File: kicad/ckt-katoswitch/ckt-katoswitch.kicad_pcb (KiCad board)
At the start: 2 copper layers, 76.2 x 63.5 mm, 50 parts, among them J1 SM04B-SRSS, J10 SM04B-SRSS, J11 Conn_AVR_TagConnect_TC2030, J2 SM04B-SRSS, J3 SM04B-SRSS, J4 SM04B-SRSS, J5 SM04B-SRSS, J6 SM04B-SRSS, J7 SM04B-SRSS, J8 SM04B-SRSS, J9 SM04B-SRSS, Q1 ZXMS6004FF, SW1 SW_DIP_x05, U1 AP7381-33Y, U2 ATtiny861A-S

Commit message: Initial cut at PCB
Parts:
- removed C10, C5, C8: 1uF, Capacitor_SMD:C_0805_2012Metric
- removed C9: 0.1uF, Capacitor_SMD:C_0805_2012Metric
- removed J10, J8, J9: SM04B-SRSS, Connector_JST:JST_SH_SM04B-SRSS-TB_1x04-1MP_P1.00mm_Horizontal
- removed J11: Conn_AVR_TagConnect_TC2030, Connector:Tag-Connect_TC2030-IDC-NL_2x03_P1.27mm_Vertical
- removed R10, R11, R6, R7, R8: 1k, Resistor_SMD:R_0805_2012Metric
- removed R9: 10k, Resistor_SMD:R_0805_2012Metric
- removed SW1: SW_DIP_x05, ISE_UltraLibrarian:CST_219SMT
- removed TP1, TP2, TP3, TP4, TP5, TP6: TestPoint, TestPoint:TestPoint_Pad_D2.0mm
- added D5: AMBER, LED_SMD:LED_0805_2012Metric, F.Cu at (34.5, 46.4)
- added D6: GREEN LED, LED_SMD:LED_0805_2012Metric, F.Cu at (70.7, 35.3)
- added D7: BLUE, LED_SMD:LED_0805_2012Metric, F.Cu at (30.6, 46.4)
- added D8: AMBER, LED_SMD:LED_0805_2012Metric, F.Cu at (65.9, 58.3)
- added JP1: SolderJumper_2_Open, Jumper:SolderJumper-2_P1.3mm_Open_RoundedPad1.0x1.5mm, F.Cu at (64.1, 63.7)
- added JP2: SolderJumper_2_Open, Jumper:SolderJumper-2_P1.3mm_Open_RoundedPad1.0x1.5mm, F.Cu at (64.1, 68.3)
- added JP3: SolderJumper_2_Open, Jumper:SolderJumper-2_P1.3mm_Open_RoundedPad1.0x1.5mm, F.Cu at (64.1, 72.9)
- added K1: AGQ200A4H, ISE_UltraLibrarian:RELAY_AGQ_A_PAN, F.Cu at (32.6, 55.5)
- added U3: ATtiny414-SS, Package_SO:SOIC-14_3.9x8.7mm_P1.27mm, F.Cu at (49.9, 54.1)
- added U4: LTV-357T, Package_SO:SO-4_4.4x3.6mm_P2.54mm, F.Cu at (59.6, 58.2)
- C1: value 10uF -> 68uF; footprint Capacitor_SMD:C_0805_2012Metric -> Capacitor_SMD:CP_Elec_6.3x5.8
- C2: value 22uF -> 10uF
- C4: value 1uF -> 22uF
- D1: value GREEN LED -> CDBM140G; footprint LED_SMD:LED_0805_2012Metric -> ISE_Generic:SOD-123T
- D2: value RED -> CDBM140G; footprint LED_SMD:LED_0805_2012Metric -> ISE_Generic:SOD-123T
- D3, D4: value AMBER -> CDBM140G; footprint LED_SMD:LED_0805_2012Metric -> ISE_Generic:SOD-123T
- J1, J2: value SM04B-SRSS -> Screw_Terminal_01x02; footprint Connector_JST:JST_SH_SM04B-SRSS-TB_1x04-1MP_P1.00mm_Horizontal -> TerminalBlock_RND:TerminalBlock_RND_205-00012_1x02_P5.00mm_Horizontal
- J3: value SM04B-SRSS -> Conn_AVR_TagConnect_TC2030; footprint Connector_JST:JST_SH_SM04B-SRSS-TB_1x04-1MP_P1.00mm_Horizontal -> Connector:Tag-Connect_TC2030-IDC-NL_2x03_P1.27mm_Vertical
- J4, J5, J6: value SM04B-SRSS -> Screw_Terminal_01x02; footprint Connector_JST:JST_SH_SM04B-SRSS-TB_1x04-1MP_P1.00mm_Horizontal -> TerminalBlock_MetzConnect:TerminalBlock_MetzConnect_Type059_RT06303HBWC_1x03_P3.50mm_Horizontal
- J7: value SM04B-SRSS -> Conn_01x03; footprint Connector_JST:JST_SH_SM04B-SRSS-TB_1x04-1MP_P1.00mm_Horizontal -> Connector_PinHeader_2.54mm:PinHeader_1x03_P2.54mm_Vertical
- Q1: value ZXMS6004FF -> DRDC3105-7
- U1: value AP7381-33Y -> AP7381-50Y
- U2: value ATtiny861A-S -> DRV8231A; footprint Package_SO:SOIC-20W_7.5x12.8mm_P1.27mm -> Package_SO:Texas_HTSOP-8-1EP_3.9x4.9mm_P1.27mm_EP2.95x4.9mm_Mask2.4x3.1mm_ThermalVias
- moved H2 67.9 mm to (29.7, 71.9)
- moved H4 64.3 mm to (71.9, 29.7)
- moved J5 55.8 mm to (36.9, 69.0), turned to 0 degrees
- moved H3 54.8 mm to (71.9, 71.9)
- moved J4 46.4 mm to (49.7, 69.0), turned to 0 degrees
- moved J7 44.2 mm to (66.3, 40.9), turned to 90 degrees
- moved D4 41.3 mm to (51.6, 34.5), turned to 180 degrees
- moved J1 37.0 mm to (64.9, 32.6), turned to 180 degrees
- moved R2 35.4 mm to (40.0, 44.7), turned to 0 degrees
- moved D3 35.0 mm to (51.6, 38.0), turned to 180 degrees
- moved J6 33.4 mm to (68.8, 53.9), turned to 90 degrees
- moved J3 33.0 mm to (42.9, 56.0), turned to 90 degrees
- moved U2 27.4 mm to (42.6, 40.1), turned to 180 degrees
- moved C4 26.2 mm to (46.9, 45.5)
- moved C3 23.1 mm to (55.8, 45.5)
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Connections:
- C2 pad 1: +3.3V -> /VIN
- C3 pad 1: /~{ISLAND_1} -> /VIN
- C4 pad 1: /~{APPR_A_1} -> +5V
- C6 pad 1: /~{ISLAND_2} -> Net-(U3-PA1)
- C7 pad 1: /~{APPR_A_2} -> Net-(U3-PA2)
- D1 pad 1: GND -> /VIN
- D1 pad 2: Net-(D1-Pad2) -> Net-(D1-A)
- D2 pad 1: GND -> /VIN
- D2 pad 2: Net-(D2-Pad2) -> Net-(D2-A)
- D3 pad 1: GND -> Net-(D2-A)
- D3 pad 2: Net-(D3-Pad2) -> GND
- D4 pad 1: GND -> Net-(D1-A)
- D4 pad 2: Net-(D4-Pad2) -> GND
- J1 pad 1: GND -> Net-(D2-A)
- J1 pad 2: /VIN -> Net-(D1-A)
- J2 pad 1: GND -> Net-(D5-K)
- J2 pad 2: /VIN -> Net-(J2-Pin_2)
- J3 pad 1: GND -> unconnected-(J3-MISO-Pad1)
- J3 pad 2: /VIN -> +5V
- J3 pad 3: Net-(J3-Pad3) -> unconnected-(J3-SCK-Pad3)
- J4 pad 1: GND -> Net-(J4-Pin_1)
- J4 pad 2: /VIN -> Net-(J4-Pin_2)
- J4 pad 3: Net-(R2-Pad1) -> Net-(J4-Pin_3)
- J5 pad 1: GND -> Net-(J5-Pin_1)
- J5 pad 2: /VIN -> Net-(J5-Pin_2)
- J5 pad 3: Net-(R2-Pad1) -> Net-(J5-Pin_3)
- J6 pad 1: GND -> Net-(J6-Pin_1)
- J6 pad 2: /VIN -> GND
- J6 pad 3: Net-(J6-Pad3) -> Net-(D8-A)
- J7 pad 1: GND -> Net-(J6-Pin_1)
- J7 pad 2: /VIN -> +5V
- J7 pad 3: Net-(J7-Pad3) -> GND
- Q1 pad 1: /~{ENABLE} -> Net-(Q1-G)
- Q1 pad 3: Net-(J1-Pad3) -> Net-(Q1-D)
- R1 pad 1: Net-(D1-Pad2) -> Net-(D6-A)
- R1 pad 2: +3.3V -> +5V
- R2 pad 1: Net-(R2-Pad1) -> Net-(D5-A)
- R2 pad 2: /~{ISLAND_1} -> Net-(J2-Pin_2)
- R3 pad 1: Net-(J3-Pad3) -> Net-(D8-K)
- R3 pad 2: /~{APPR_A_1} -> Net-(J6-Pin_1)
- R4 pad 1: Net-(J6-Pad3) -> Net-(U3-PA1)
- R4 pad 2: /~{APPR_B_1} -> Net-(J6-Pin_1)
- R5 pad 1: Net-(D2-Pad2) -> Net-(U3-PA2)
- R5 pad 2: /~{ENABLE} -> Net-(D8-A)
- U1 pad 1: +3.3V -> +5V
- U2 pad 1: /AVR_MOSI -> GND
- U2 pad 2: /AVR_MISO -> Net-(U2-IN2)
- U2 pad 3: /AVR_SCK -> Net-(U2-IN1)
- U2 pad 4: /~{ENABLE} -> +5V
- U2 pad 5: +3.3V -> /VIN
- U2 pad 6: GND -> Net-(D5-K)
- U2 pad 7: /~{APPR_A_2} -> GND
- U2 pad 8: /~{ISLAND_2} -> Net-(J2-Pin_2)
- U2 pad 9: /~{APPR_B_2} -> GND
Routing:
- net /VIN: track 184.8 -> 23.1 mm
- net +5V: track 0.00 -> 81.1 mm, vias 0 -> 2
- net +3.3V: track 77.0 -> 0.00 mm
- net GND: track 123.3 -> 47.5 mm, vias 68 -> 27
- net /~{RESET}: track 45.9 -> 0.00 mm, vias 2 -> 0
- net Net-(J1-Pad3): track 45.9 -> 0.00 mm, vias 4 -> 0
- net Net-(J6-Pin_1): track 0.00 -> 45.0 mm
- net /AVR_MOSI: track 43.0 -> 0.00 mm, vias 2 -> 0
- net Net-(J3-Pad3): track 39.0 -> 0.00 mm, vias 1 -> 0
- net /~{ENABLE}: track 36.3 -> 0.00 mm
- net Net-(R2-Pad1): track 34.7 -> 0.00 mm, vias 1 -> 0
- net /AVR_MISO: track 32.8 -> 0.00 mm, vias 2 -> 0
- net Net-(J8-Pad3): track 31.3 -> 0.00 mm, vias 1 -> 0
- net Net-(J7-Pad3): track 30.9 -> 0.00 mm, vias 1 -> 0
- net Net-(JP3-B): track 0.00 -> 30.8 mm
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- added copper zone on F.Cu, net /VIN
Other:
- board size 76.2 x 63.5 mm -> 50.8 x 50.8 mm
- board text added: "CKT-KATOSWITCH v1.0"
- board text added: "CONFIG SOLDER JUMPERS"
- board text added: "G"
- board text added: "INPUTS"
- board text added: "Iowa Scaled Eng. CC BY-SA ©2026"
- board text added: "N"
- board text added: "POSITION CONTACTS"
- board text added: "PWR"
- board text added: "R"
- board text added: "TT"
- board text added: "TURNOUT"
- board text removed: "*"
- board text removed: "ACTIVE"
- board text removed: "APPROACH"
- board text removed: "CKT-XING-TXM v1.0 CC BY-SA"
- board text removed: "CROSSING EXPANSION"
- board text removed: "For Approach & Island Timeout Settings, See Manual"
- board text removed: "ISLAND"
- board text removed: "LEFT APPROACH"
- board text removed: "LEFT ISLAND"
- board text removed: "ON/1"
- board text removed: "RIGHT APPROACH"
- board text removed: "RIGHT ISLAND"
- board text removed: "RoadReady Expansion Module"
- board text removed: "TIMEOUTS"
- board text removed: "TRACK A SENSOR INPUTS"
- board text removed: "TRACK B SENSOR INPUTS"
- board text removed: "TRK A ACTIVE"
- board text removed: "TRK B ACTIVE"
- board text removed: "X"
- board text removed: "Y"
- board text removed: "www.iascaled.com"
- board text removed: "©2024"

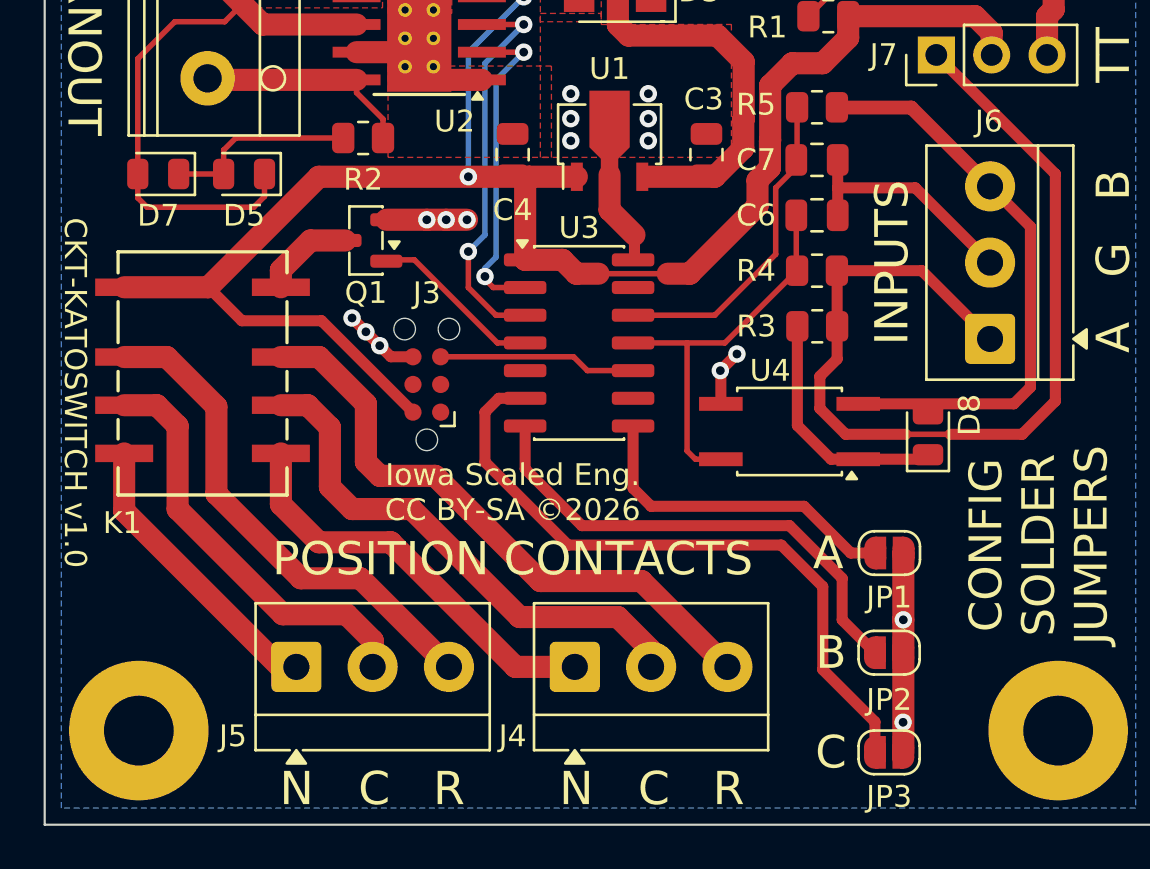
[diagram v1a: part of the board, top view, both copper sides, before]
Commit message: Updates to add "switch reverse" indicator
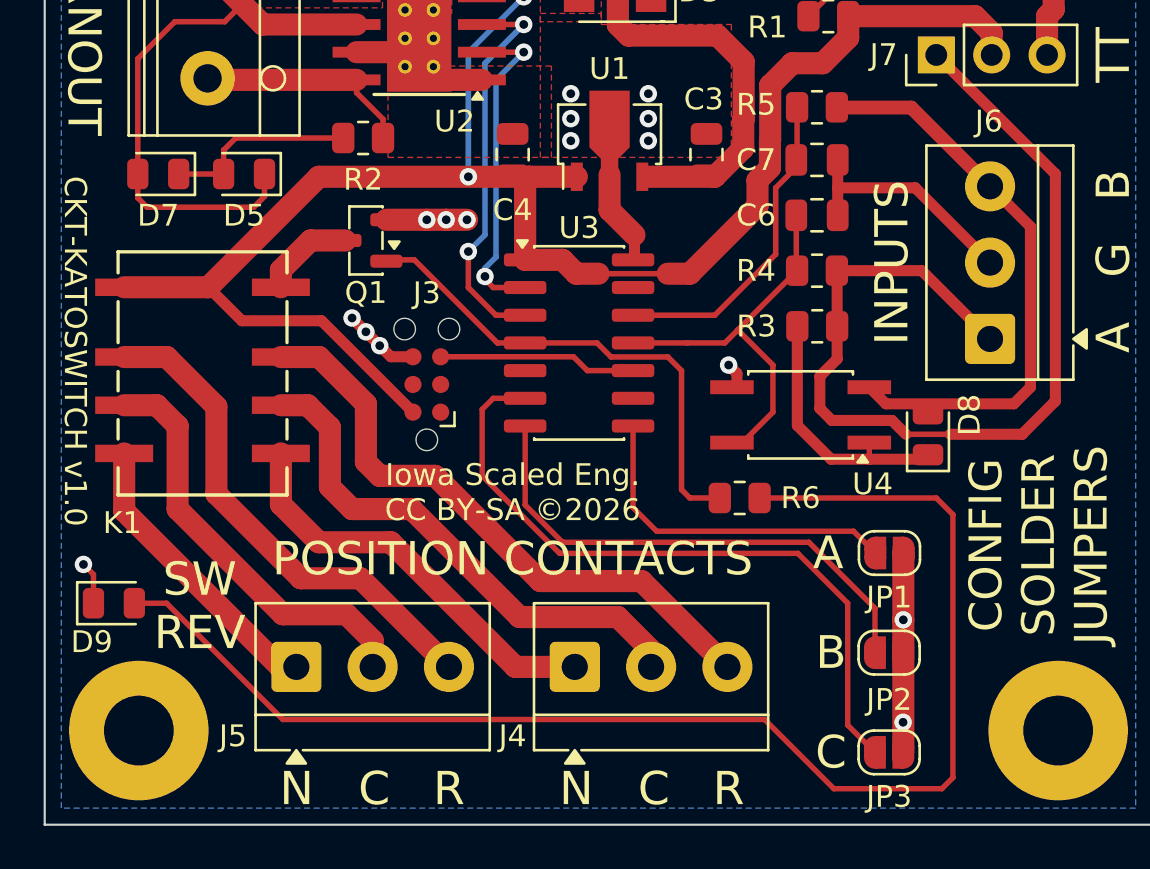
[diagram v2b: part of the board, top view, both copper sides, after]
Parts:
- added D9: AMBER, LED_SMD:LED_0805_2012Metric, F.Cu at (28.6, 66.0)
- added R6: 1k, Resistor_SMD:R_0805_2012Metric, F.Cu at (57.3, 61.2)
- moved U4 0.92 mm to (60.1, 57.4)
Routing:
- net Net-(D9-A): track 0.00 -> 62.5 mm
- net Net-(Q1-G): track 7.97 -> 23.0 mm
- net Net-(JP2-B): track 22.6 -> 23.7 mm
- net Net-(JP3-B): track 30.8 -> 31.8 mm
- net Net-(JP1-B): track 15.2 -> 15.8 mm
- net GND: track 47.5 -> 48.1 mm
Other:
- board text added: "SW REV"

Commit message: Clean up a couple small DRCs
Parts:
- R1: value 1k -> 10k
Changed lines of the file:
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@@
 			)
 		)
-		(property "Value" "1k"
+		(property "Value" "10k"
 			(at 0 1.65 0)
 			(layer "F.Fab")
